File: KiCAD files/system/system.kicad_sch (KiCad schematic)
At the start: 14 parts, among them J1 Input, J2 Conn_01x04_Female, SW1 SW_Push, U1 ATmega328P-P, Y1 Crystal

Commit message: Update schematics of system
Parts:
- added R?: 10kR, Resistor_THT:R_Axial_DIN0207_L6.3mm_D2.5mm_P10.16mm_Horizontal, symbol Device:R
- added R?: 5.1kR, Resistor_THT:R_Axial_DIN0207_L6.3mm_D2.5mm_P10.16mm_Horizontal, symbol Device:R
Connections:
- net +5V: now also R?.1; no longer C1.1, R1.2, U1.20 (AVCC), U1.7 (VCC)
- net GND: now also R?.2
- new net +3.3V: C1.1, R1.2, R?.1, R?.2, U1.20 (AVCC), U1.7 (VCC)
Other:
- moved on the sheet: J1

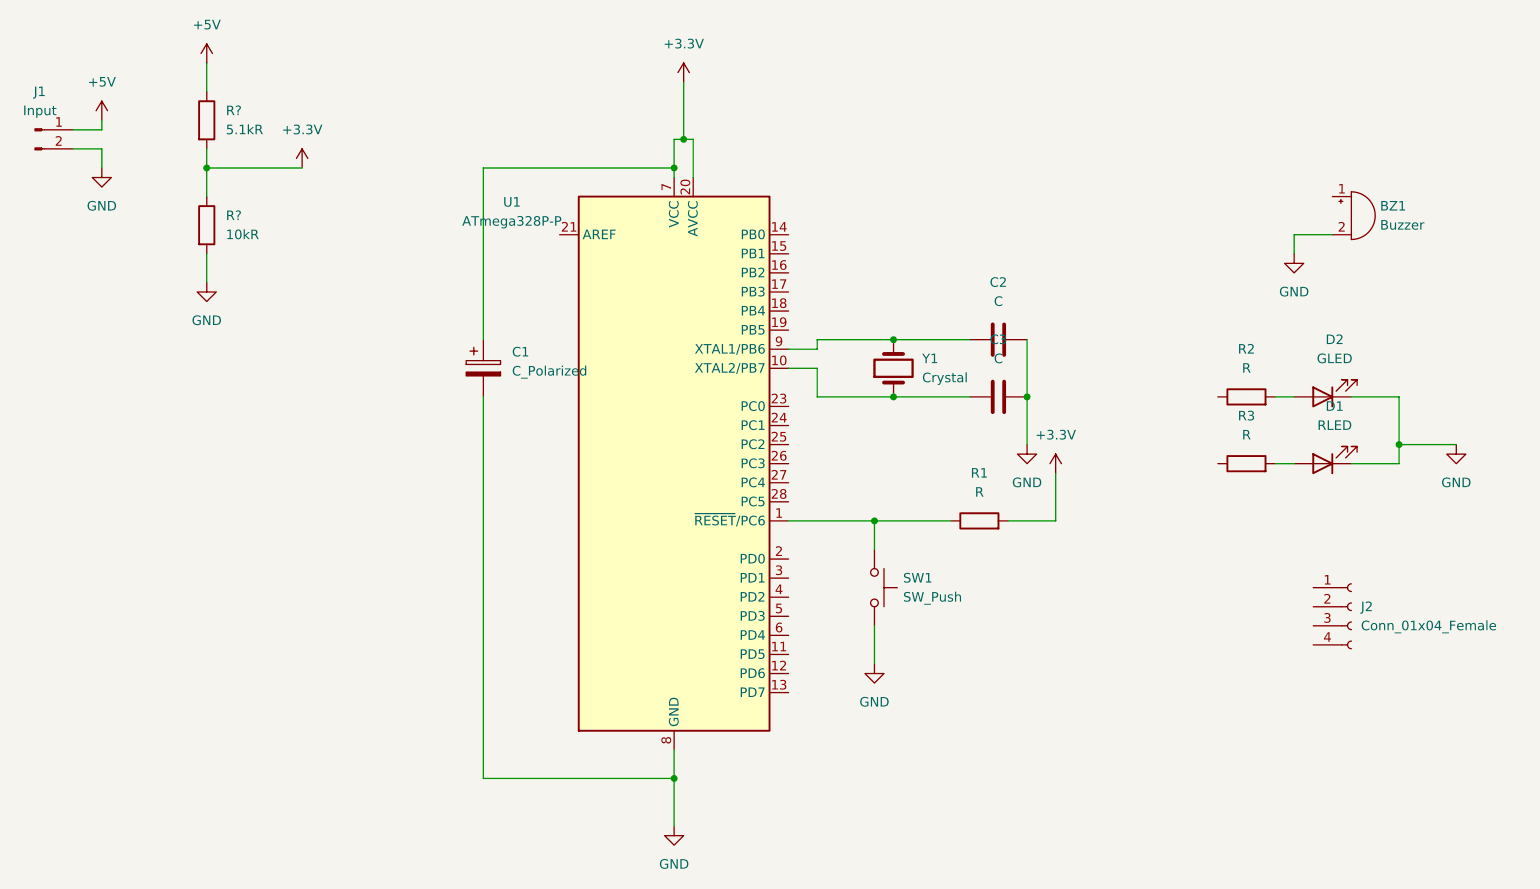
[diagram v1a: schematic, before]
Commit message: edited the system side circuit
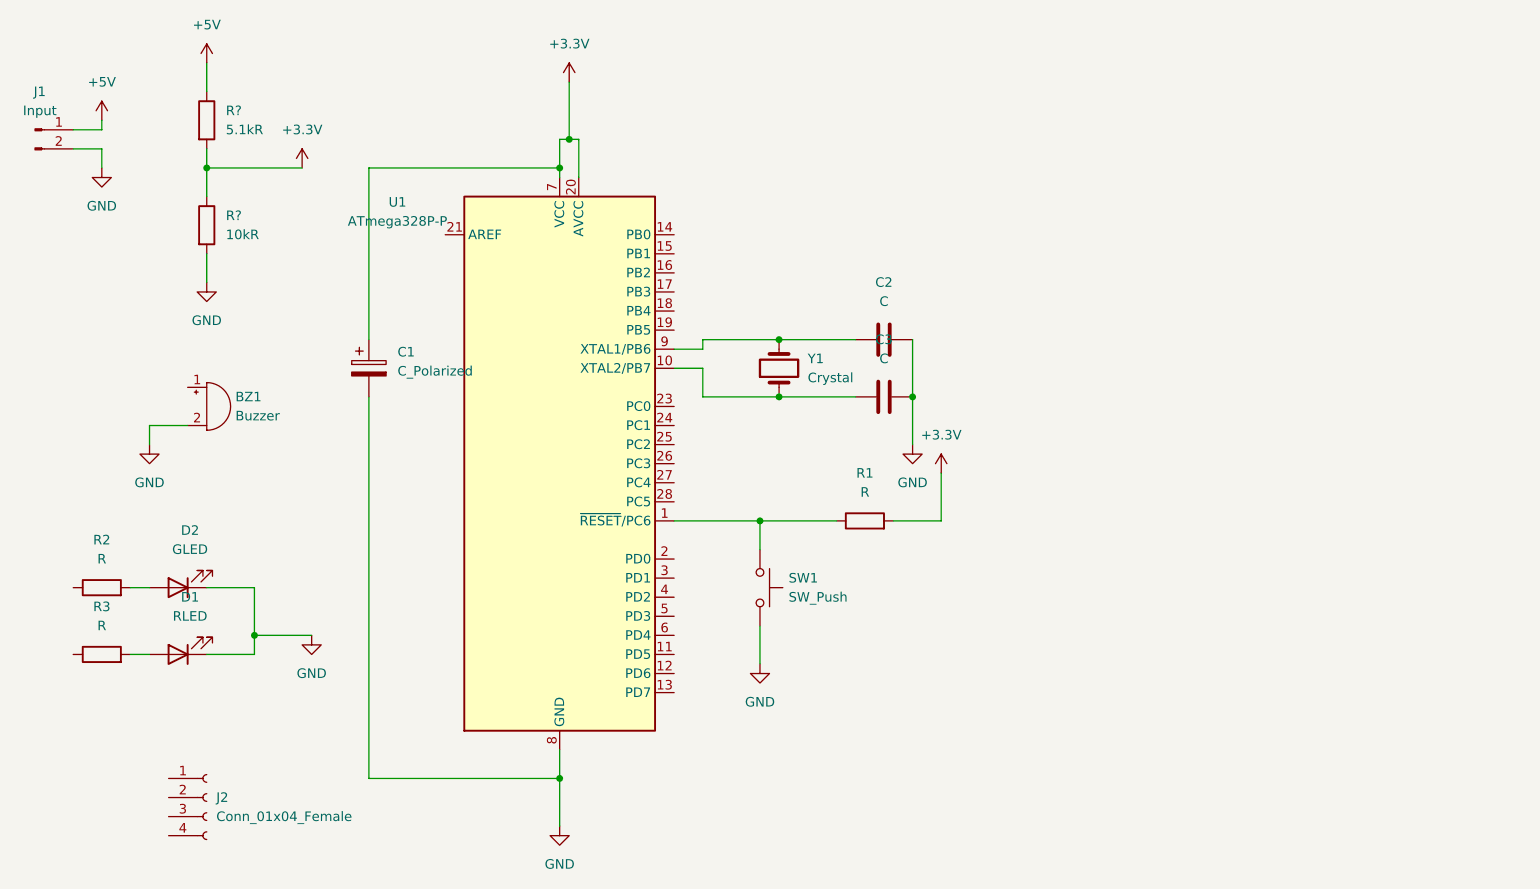
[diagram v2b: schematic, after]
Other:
- moved on the sheet: BZ1, C1, C2, C3, D1, D2, J2, R1, R2, R3, SW1, U1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
